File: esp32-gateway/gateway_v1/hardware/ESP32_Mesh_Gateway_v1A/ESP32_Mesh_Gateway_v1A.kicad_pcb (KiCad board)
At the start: 2 copper layers, 70 x 50 mm, 25 parts, among them J1 Ext Power, U1 ESP32-S3 Super Mini, U2 ESP32-C3 Super Mini, U3 BME280

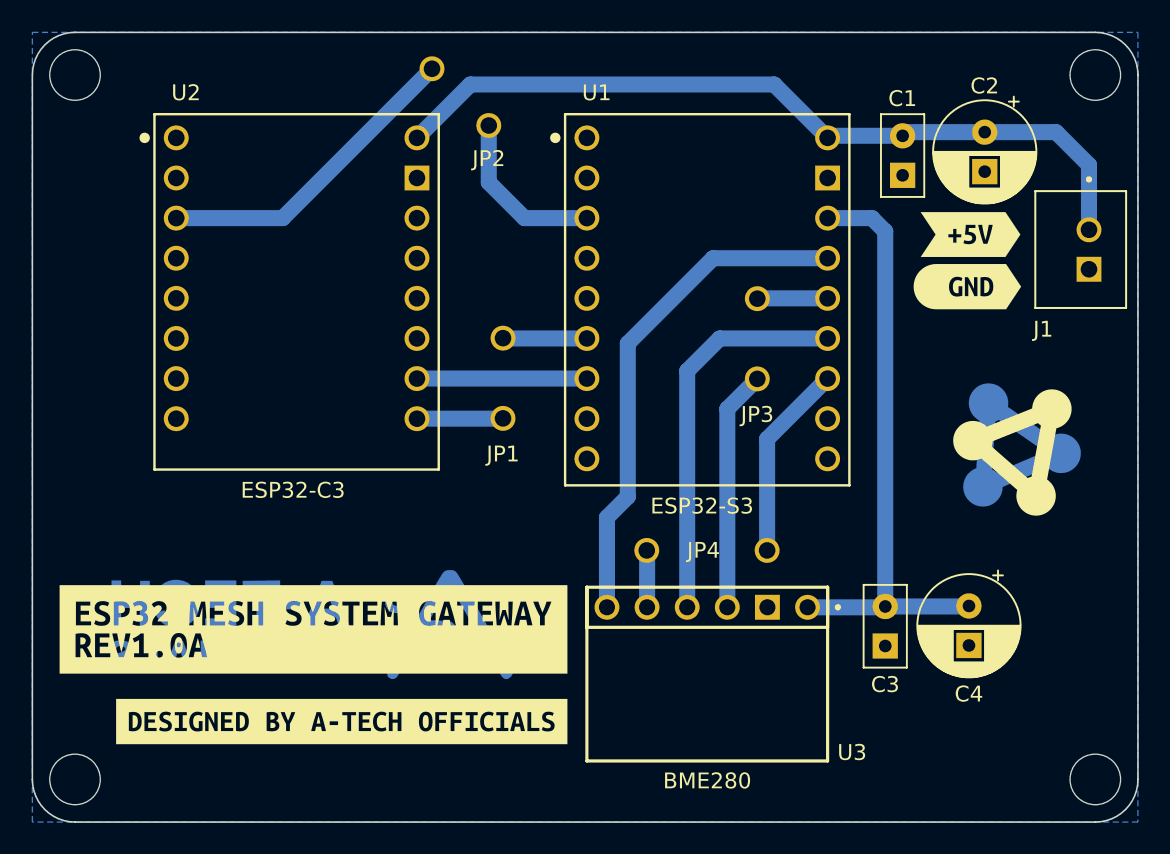
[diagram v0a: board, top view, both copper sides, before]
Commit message: feat: improve node discovery, add new gateway PCB variants, and document C3 Super Mini RF fixes
- polish gateway and node discovery behavior so pairing candidates appear faster and stale "available to pair" entries clear more predictably
- document the new Gateway v1A-v1D single-layer THT PCB variants for these board combinations:
  - v1A: Seeed Studio XIAO ESP32-S3 + ESP32-C3 Super Mini
  - v1B: Seeed Studio XIAO ESP32-S3 + Seeed Studio XIAO ESP32-C3
  - v1C: Seeed Studio XIAO ESP32-S3 + DFRobot Beetle ESP32-C3
  - v1D: Waveshare ESP32-S3-DevKit-C-N8R8 + ESP32-C3 Super Mini
- note that all new gateway PCB variants include connection points for a future BME280 module
- deprecate the earlier ESP32-S3 Super Mini based gateway PCB because its 4 MB flash is not suitable for the current gateway firmware line
- document the introduction of user_config.h as the new home for user-configurable firmware definitions across gateway and node projects
- document the ESP32-C3 Super Mini specific WiFi transmit power limit behavior and note that it must be applied only after WiFi startup
- bump documented firmware versions:
  - gateway main firmware: v2.1.4 -> v2.2.0
  - gateway coprocessor firmware: v0.1.1 -> v0.2.0
  - sensor node firmware: v2.1.4 -> v2.2.0
  - relay node firmware: v1.2.2 -> v1.3.0
  - hybrid relay node firmware: v0.1.3 -> v0.2.0
  - user_config.h: v1.0.0 introduced
- add a dedicated ESP32-C3 Super Mini WiFi test report with the full receive/transmit test tables from Test-1 to Test-12
- summarize the documented RF findings:
  - some Super Mini boards had weak or unstable onboard LDOs
  - stock ceramic antenna performance was poor
  - LDO replacement and antenna changes improved several boards
  - the 8.5 dBm TX cap helped stabilize marginal boards
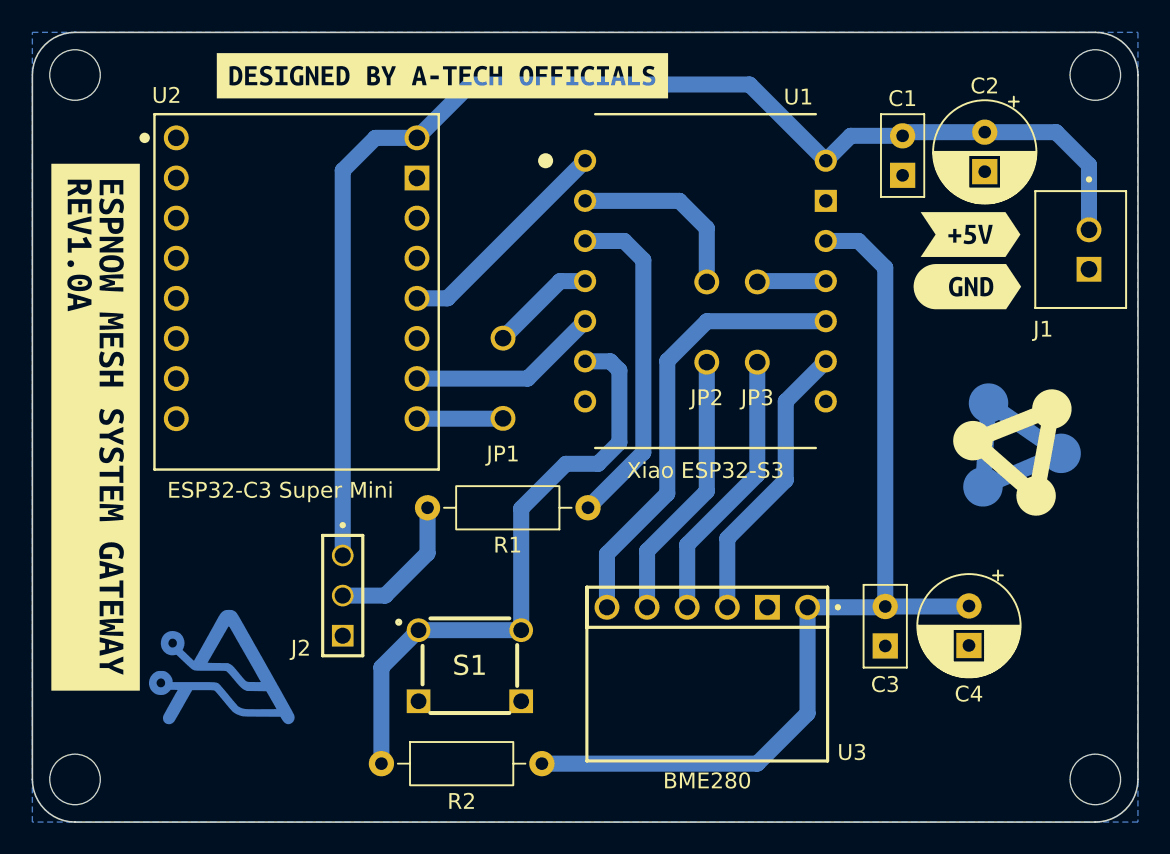
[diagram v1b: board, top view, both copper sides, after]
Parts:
- removed the G*** at (132.1, 77.4) (x2)
- removed JP4: 2H_Jumper_P7.62mm, Jumpers:2H_Jumper_P7.62mm
- removed kibuzzard-69C033F4: G***, kibuzzard-69C033F4
- added G***: LOGO, A-Tech_Officials:A-Tech_Officials_Logo_2025_10mm, B.Cu at (126.7, 80.1)
- added G***: LOGO, A-Tech_Officials:A-Tech_Officials_Logo_2025_10mm_mask, B.Cu at (126.7, 80.1)
- added J2: RGB LED, TSW-103-07-G-S:SAMTEC_TSW-103-07-G-S, F.Cu at (135.8, 71.5)
- added R1: 100R, Resistor_THT:R_Axial_DIN0207_L6.3mm_D2.5mm_P10.16mm_Horizontal, F.Cu at (149.8, 70.0)
- added R2: 10K, Resistor_THT:R_Axial_DIN0207_L6.3mm_D2.5mm_P10.16mm_Horizontal, F.Cu at (136.7, 86.2)
- added S1: RST BTN, FSM10JH:FSM4JH, F.Cu at (142.3, 80.0)
- added kibuzzard-69CC272A: G***, kibuzzard-69CC272A, F.Cu at (115.8, 64.9)
- U1: value ESP32-S3 Super Mini -> XIAO-ESP32-S3-DIP; footprint Development_Boards:ESP32-S3_Super_Mini -> XIAO_Series_Boards:Xiao ESP32-S3 THT
- moved kibuzzard-69C035C1 38.9 mm to (140.3, 44.1)
- moved JP2 17.2 mm to (158.3, 54.6), turned to 90 degrees
- moved U1 16.1 mm to (150.2, 45.1)
- moved JP3 1.06 mm to (160.5, 60.8)
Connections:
- C1 pad 1: VIN -> +5V
- C2 pad 1: VIN -> +5V
- J1 pad 1: VIN -> +5V
- JP1 pad 1: TX -> RXD1
- JP1 pad 2: TX -> RXD1
- JP2 pad 1: HELPER_RST -> BMP_CS
- JP2 pad 2: HELPER_RST -> BMP_CS
- JP3 pad 1: SCK -> MOSI
- JP3 pad 2: SCK -> MOSI
- U1 pad 1: unconnected-(U1-GPIO43/TXD0-Pad1) -> HELPER_RST
- U1 pad 10: unconnected-(U1-ADC1_7/GPIO8-Pad10) -> MISO
- U1 pad 11: unconnected-(U1-FSPIHD/GPIO9-Pad11) -> MOSI
- U1 pad 12: BMP_CS -> +3.3V
- U1 pad 13: MOSI -> GND
- U1 pad 14: SCK -> +5V
- U1 pad 2: unconnected-(U1-GPIO44/RXD0-Pad2) -> BMP_CS
- U1 pad 3: HELPER_RST -> ARGB_LED
- U1 pad 4: unconnected-(U1-GPIO2/ADC1_1-Pad4) -> RXD1
- U1 pad 5: unconnected-(U1-GPIO3/JTAG-Pad5) -> RXD0
- U1 pad 6: TX -> FR_BTN
- U1 pad 7: RX -> unconnected-(U1-GPIO43_D6_TX-Pad7)
- U1 pad 9: unconnected-(U1-GPIO7/ADC1_6-Pad9) -> SCK
- U2 pad 10: RX -> RXD0
- U2 pad 12: unconnected-(U2-ADC3/GPIO3-Pad12) -> HELPER_RST
- U2 pad 16: VIN -> +5V
- U2 pad 3: HELPER_RST -> unconnected-(U2-GPIO7/SS-Pad3)
- U2 pad 9: TX -> RXD1
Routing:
- net +5V: track 0.00 -> 81.6 mm
- net VIN: track 50.5 -> 0.00 mm
- net FR_BTN: track 0.00 -> 38.5 mm
- net +3.3V: track 38.0 -> 61.0 mm
- net ARGB_LED: track 0.00 -> 21.3 mm
- net HELPER_RST: track 30.9 -> 14.3 mm
- net BMP_CS: track 16.1 -> 28.9 mm
- net RXD0: track 0.00 -> 12.1 mm
- net RXD1: track 0.00 -> 12.1 mm
- net TX: track 10.8 -> 0.00 mm
- net RX: track 10.8 -> 0.00 mm
- net Net-(J2-Pad02): track 0.00 -> 9.36 mm
- net MISO: track 32.1 -> 28.3 mm
- net MOSI: track 24.7 -> 21.7 mm
- net SCK: track 19.7 -> 18.2 mm
